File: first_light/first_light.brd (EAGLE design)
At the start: 160 x 100 mm, 56 parts, among them IC1 MC34063AD, J1 DCJ0202, J2 DCJ0202, Q1 ZXMN4A06GTA, U1 STM32F051C6T6, X1 8MHz, Y1 32.768kHz

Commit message: more layout work
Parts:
- moved R7 75.5 mm to (44.6, 72.4), turned to 270 degrees
- moved R11 74.7 mm to (65.0, 69.6)
- moved R12 74.7 mm to (70.5, 69.6)
- moved T2 74.7 mm to (66.5, 72.6)
- moved T3 74.7 mm to (71.9, 72.6)
- moved R10 74.7 mm to (59.6, 69.6)
- moved R13 74.7 mm to (48.9, 69.6)
- moved R8 74.7 mm to (42.5, 72.5)
- moved R9 74.7 mm to (54.2, 69.6)
- moved T1 74.7 mm to (61.1, 72.6)
- moved T4 74.7 mm to (55.7, 72.6)
- moved T5 74.7 mm to (50.3, 72.6)
- moved R2 74.6 mm to (62.8, 89.7)
- moved R3 74.6 mm to (60.2, 89.7)
- moved R4 74.6 mm to (57.7, 89.7)
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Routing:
- net +12V: track 0.00 -> 162.8 mm
- net SSD_B: track 0.00 -> 50.5 mm
- net SSD_G: track 0.00 -> 46.3 mm
- net SSD_A: track 0.00 -> 42.3 mm
- net SSD_C: track 0.00 -> 38.2 mm
- net SSD_L1L2: track 0.00 -> 33.9 mm
- net SSD_F: track 0.00 -> 29.5 mm
- net N$8: track 0.00 -> 24.2 mm
- net N$32: track 0.00 -> 23.7 mm
- net +3V3: track 0.00 -> 17.1 mm
- net N$7: track 0.00 -> 15.9 mm
- net N$28: track 0.00 -> 8.44 mm
- net N$10: track 0.00 -> 7.08 mm
- net N$29: track 0.00 -> 5.98 mm
- net N$13: track 0.00 -> 5.16 mm
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- added copper zone on layer 1, net SWITCH

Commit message: layout work
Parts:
- moved C5 82.0 mm to (122.2, 91.2), turned to 90 degrees
- moved C4 75.4 mm to (117.1, 91.2), turned to 90 degrees
- moved S1 68.3 mm to (117.1, 69.7), turned to 90 degrees
- moved C3 68.2 mm to (112.0, 90.0), turned to 90 degrees
- moved C9 68.1 mm to (114.5, 83.6), turned to 90 degrees
- moved C2 65.8 mm to (114.5, 77.3), turned to 90 degrees
- moved C10 61.3 mm to (109.5, 83.6), turned to 90 degrees
- moved C1 58.8 mm to (109.5, 77.3), turned to 90 degrees
- moved JP1 58.5 mm to (100.6, 95.0), turned to 180 degrees
- moved U1 49.9 mm to (101.8, 81.1), turned to 90 degrees
- moved X1 48.6 mm to (103.1, 67.1), turned to 180 degrees
- moved Y1 39.9 mm to (96.8, 72.2), turned to 90 degrees
- moved R16 35.5 mm to (91.1, 80.2), turned to 180 degrees
- moved R15 32.9 mm to (86.6, 83.6), turned to 180 degrees

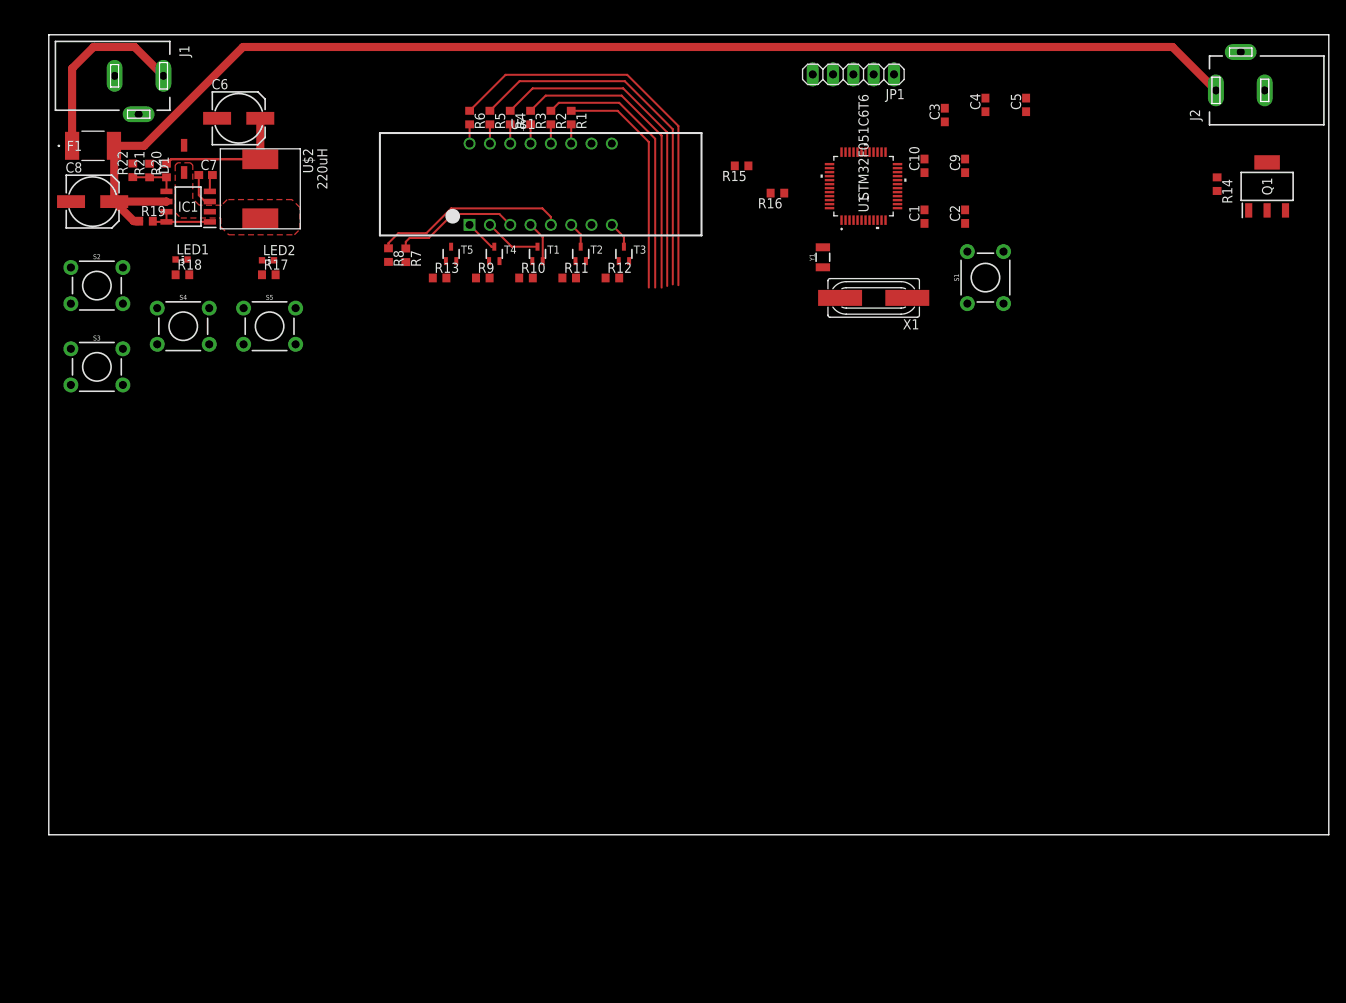
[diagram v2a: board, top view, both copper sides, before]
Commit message: now using esp32 due to no stm available
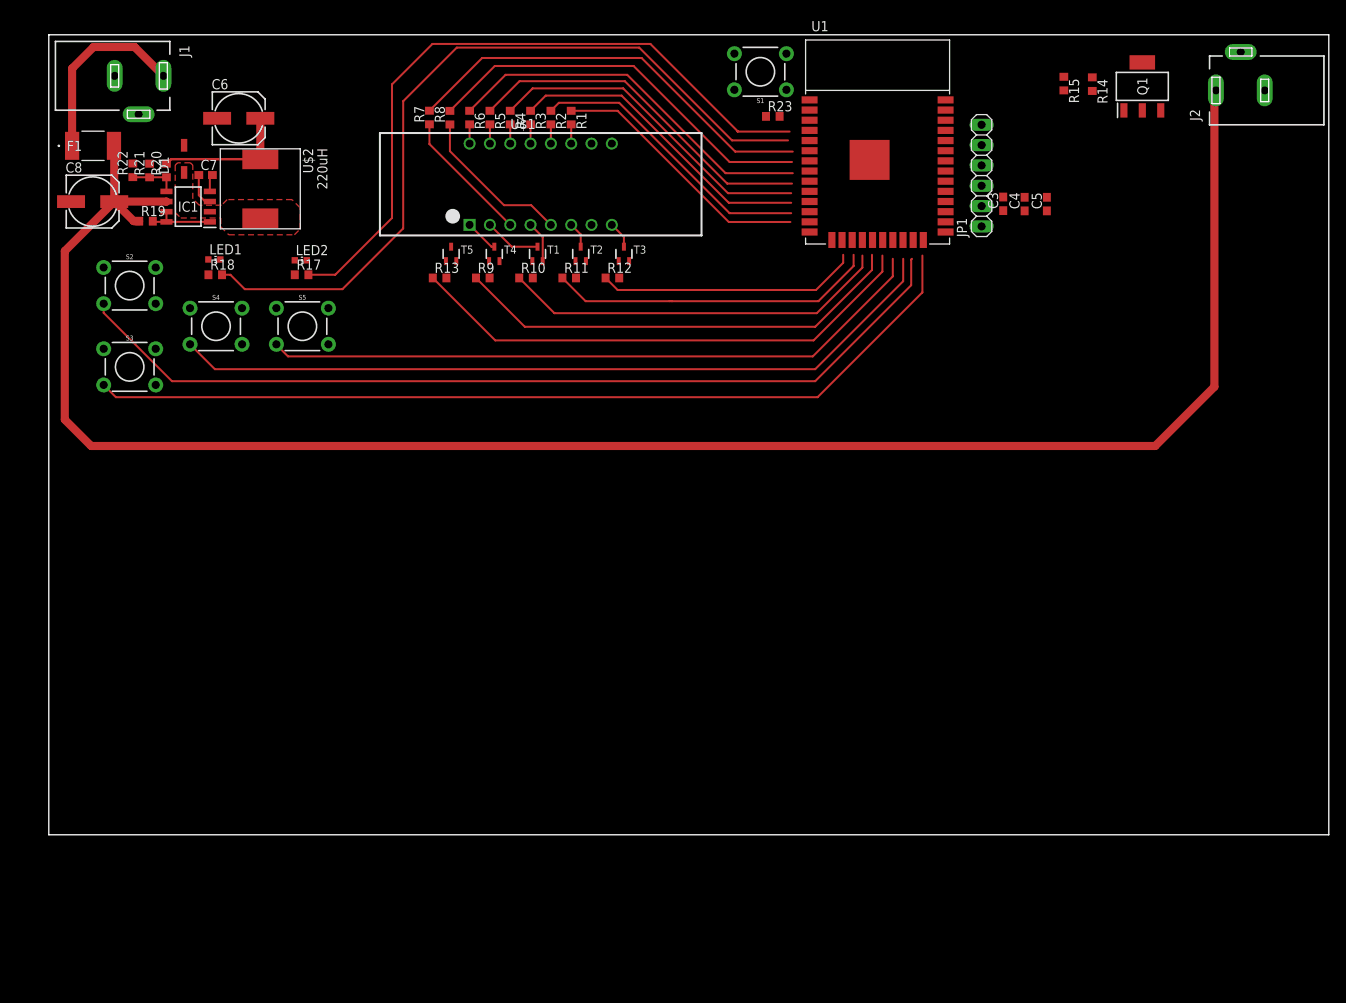
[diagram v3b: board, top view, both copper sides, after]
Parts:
- removed C1, C10, C2, C9: 10pF, rcl:C0603
- removed R16: 10k, rcl:R0603
- removed X1: 8MHz, IQD-Frequency-Products:HC49-4-HSMX
- removed Y1: 32.768kHz, SparkFun-Clocks:CRYSTAL-SMD-3.2X1.5MM
- added R23: 10k, rcl:R0603
- JP1: device pinhead:1X05 -> pinhead:1X06
- U1: value STM32F051C6T6 -> ESP32-WROOM-32D; device STM32F051C6:LQFP48-7X7MM -> ESP32-WROOM-32D:MODULE_ESP32-WROOM-32D
- moved R15 41.6 mm to (126.9, 93.9), turned to 270 degrees
- moved S1 38.1 mm to (89.0, 95.4), turned to 180 degrees
- moved JP1 20.4 mm to (116.6, 82.4), turned to 90 degrees
- moved Q1 20.0 mm to (136.7, 93.5)
- moved R14 20.0 mm to (130.4, 93.8)
- moved R8 18.8 mm to (50.1, 89.6), turned to 90 degrees
- moved R7 17.5 mm to (47.6, 89.7), turned to 90 degrees
- moved C4 13.3 mm to (122.0, 78.8)
- moved C3 13.3 mm to (119.3, 78.9)
- moved C5 12.7 mm to (124.8, 78.8)
- moved U1 5.79 mm to (103.6, 86.6), turned to 0 degrees
- moved LED1 4.10 mm to (20.7, 71.9)
- moved LED2 4.10 mm to (31.5, 71.8)
- moved R17 4.10 mm to (31.6, 70.0)
- moved R18 4.10 mm to (20.8, 70.0)
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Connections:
- removed net N$14: C1.1, U1.6, X1.1
- removed net N$20: C2.1, U1.5, X1.2
- removed net N$25: R16.1, U1.44
- removed net N$30: C9.1, U1.4, Y1.P$1
- removed net N$31: C10.1, U1.3, Y1.P$2
- removed net SWCLK: JP1.3, U1.37
- removed net SWDIO: JP1.2, U1.34
- removed net VBAT: U1.1
- new net IO0: JP1.4
- new net RXD0: JP1.5, U1.34
- new net TXD0: JP1.6, U1.35
- net !RST: now also R23.1, U1.3; no longer U1.7
- net +3V3: now also JP1.2, R23.2, U1.2; no longer JP1.4, U1.24, U1.48, U1.9
- net BTN_DN: now also U1.24; no longer U1.12
- net BTN_L: now also U1.22; no longer U1.11
- net BTN_R: now also U1.21; no longer U1.10
- net BTN_UP: now also U1.23; no longer U1.13
- net GND: now also JP1.3, U1.1, U1.15, U1.38, U1.39; no longer C1.2, C10.2, C2.2, C9.2, JP1.5, R16.2, U1.23, U1.47, U1.8
- net LED_ALM: now also U1.5; no longer U1.15
- net LED_SET: now also U1.4; no longer U1.14
- net SSD_A: now also U1.10; no longer U1.42
- net SSD_B: now also U1.8; no longer U1.40
- net SSD_BLANK: now also U1.20
- net SSD_C: now also U1.11; no longer U1.43
- net SSD_D1: now also U1.19
- net SSD_D2: now also U1.18
- net SSD_D3: now also U1.17
- net SSD_D4: now also U1.16
- net SSD_F: now also U1.13; no longer U1.46
- net SSD_G: now also U1.9; no longer U1.41
- net SSD_L1L2: now also U1.12; no longer U1.45
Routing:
- net BTN_UP: track 0.00 -> 113.9 mm
- net BTN_DN: track 0.00 -> 113.0 mm
- net LED_ALM: track 0.00 -> 98.1 mm
- net BTN_L: track 0.00 -> 97.8 mm
- net LED_SET: track 0.00 -> 86.5 mm
- net BTN_R: track 0.00 -> 84.1 mm
- net +12V: track 162.8 -> 232.7 mm
- net SSD_BLANK: track 0.00 -> 65.0 mm
- net SSD_D1: track 0.00 -> 56.9 mm
- net SSD_D: track 0.00 -> 53.0 mm
- net SSD_E: track 0.00 -> 50.1 mm
- net SSD_D2: track 0.00 -> 48.6 mm
- net SSD_D3: track 0.00 -> 40.8 mm
- net SSD_D4: track 0.00 -> 32.7 mm
- net N$8: track 24.2 -> 19.8 mm
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
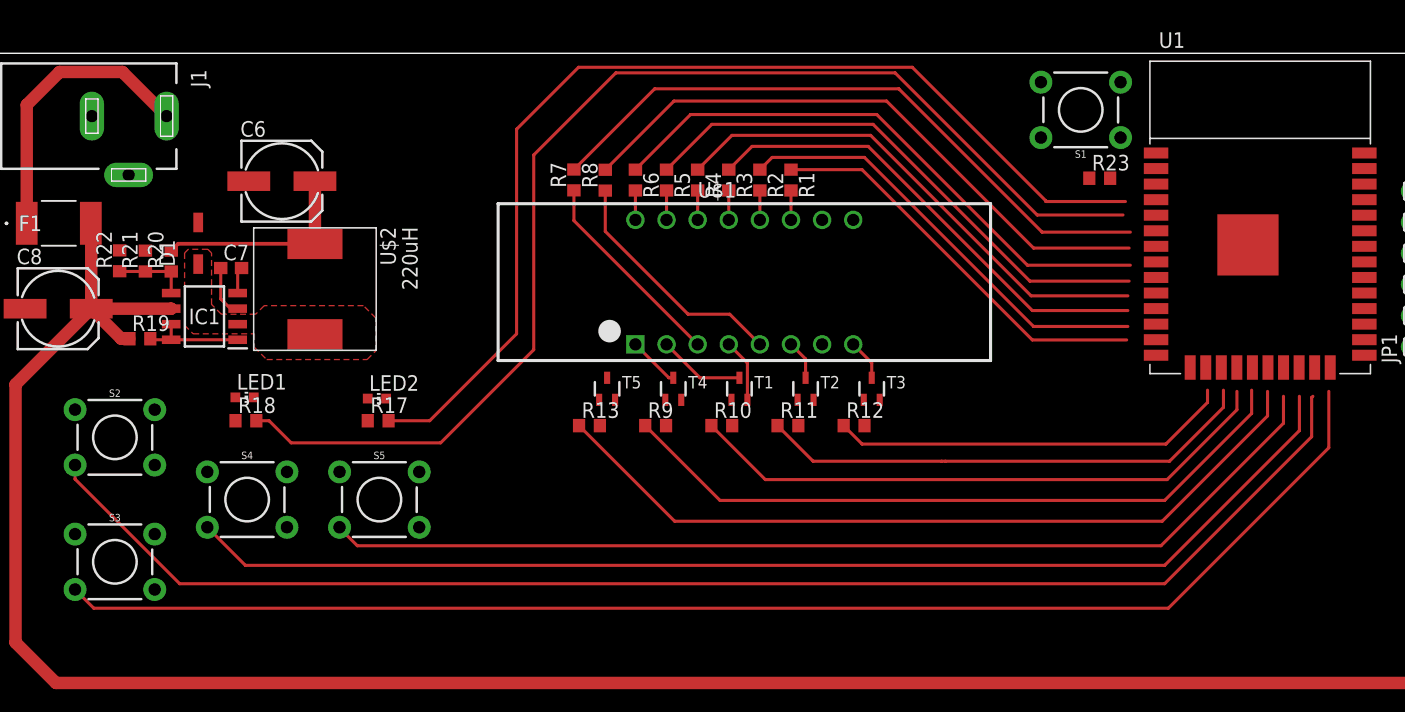
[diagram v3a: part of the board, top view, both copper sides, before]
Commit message: wired up ssd to esp
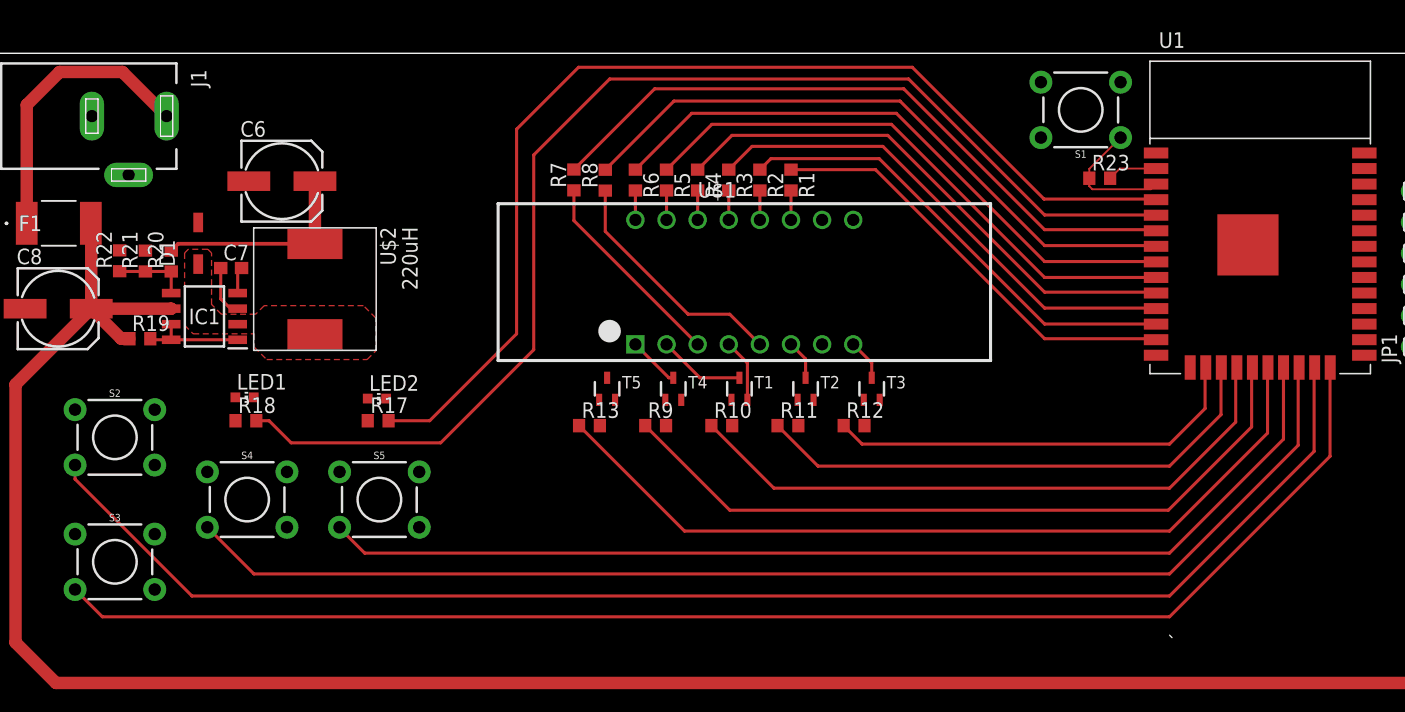
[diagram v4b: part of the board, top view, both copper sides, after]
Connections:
- net SSD_D: now also U1.6
- net SSD_E: now also U1.7
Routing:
- net !RST: track 0.00 -> 10.8 mm
- net +3V3: track 17.1 -> 21.1 mm
- net BTN_UP: track 113.9 -> 118.0 mm
- net BTN_R: track 84.1 -> 87.7 mm
- net BTN_L: track 97.8 -> 101.4 mm
- net SSD_BLANK: track 65.0 -> 68.4 mm
- net SSD_D1: track 56.9 -> 60.1 mm
- net SSD_D2: track 48.6 -> 51.6 mm
- net BTN_DN: track 113.0 -> 116.0 mm
- net LED_SET: track 86.5 -> 88.9 mm
- net SSD_F: track 33.2 -> 35.5 mm
- net SSD_D3: track 40.8 -> 43.2 mm
- net LED_ALM: track 98.1 -> 100.4 mm
- net SSD_C: track 38.9 -> 41.2 mm
- net SSD_A: track 41.7 -> 43.9 mm
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
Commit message: last adjustments before new layout
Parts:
- moved J2 105.8 mm to (87.7, 6.85)
- moved R14 88.8 mm to (88.5, 15.5)
- moved Q1 86.6 mm to (95.0, 17.6)
- moved R15 80.8 mm to (100.4, 17.6)
- moved C4 56.5 mm to (101.3, 26.2)
- moved C3 49.2 mm to (100.0, 33.6)
- moved JP1 49.2 mm to (97.3, 37.1)
- moved U1 49.2 mm to (84.3, 41.3)
- moved LED1 48.2 mm to (18.4, 23.8)
- moved S2 48.2 mm to (7.81, 20.6)
- moved S3 48.2 mm to (7.81, 10.4)
- moved S4 48.2 mm to (18.6, 15.5)
- moved S5 48.2 mm to (29.4, 15.5)
- moved LED2 48.2 mm to (29.2, 23.7)
- moved R17 48.2 mm to (29.3, 21.9)
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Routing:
- net +12V: track 232.7 -> 132.1 mm
- net BTN_UP: track 118.0 -> 100.9 mm
- net BTN_R: track 87.7 -> 70.6 mm
- net BTN_L: track 101.4 -> 84.3 mm
- net BTN_DN: track 116.0 -> 99.0 mm
- net LED_SET: track 88.9 -> 76.2 mm
- net LED_ALM: track 100.4 -> 87.7 mm
- net SSD_D2: track 51.6 -> 40.1 mm
- net SSD_D4: track 34.7 -> 23.1 mm
- net SSD_BLANK: track 68.4 -> 56.9 mm
- net SSD_D3: track 43.2 -> 31.6 mm
- net SSD_D1: track 60.1 -> 48.5 mm
- net SSD_F: track 35.5 -> 24.9 mm
- net SSD_D: track 55.1 -> 44.5 mm
- net SSD_E: track 52.2 -> 41.8 mm
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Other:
- board size 160 x 100 mm -> 100 x 55 mm

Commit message: working on new layout
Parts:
- moved R15 92.9 mm to (13.5, -15.2)
- moved J2 85.2 mm to (3.85, -8.49), turned to 0 degrees
- moved Q1 79.7 mm to (20.2, -9.85)
- moved R14 77.2 mm to (14.0, -4.77)
- moved JP1 56.8 mm to (47.7, 9.40), turned to 270 degrees
- moved U1 46.6 mm to (52.5, 7.20), turned to 180 degrees
- moved R7 20.1 mm to (53.3, 30.0), turned to 270 degrees
- moved R6 18.3 mm to (55.7, 30.1), turned to 90 degrees
- moved R5 18.2 mm to (58.2, 30.1), turned to 90 degrees
- moved R4 18.2 mm to (60.7, 30.1), turned to 90 degrees
- moved R3 18.2 mm to (63.2, 30.1), turned to 90 degrees
- moved R2 18.2 mm to (65.7, 30.1), turned to 90 degrees
- moved R1 18.1 mm to (68.2, 30.1), turned to 90 degrees
- moved R8 16.9 mm to (51.1, 30.1), turned to 270 degrees
- moved T3 15.8 mm to (48.4, 32.7)
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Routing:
- net +12V: track 132.1 -> 26.4 mm
- net BTN_DN: track 99.0 -> 0.00 mm
- net BTN_UP: track 100.9 -> 12.5 mm
- net BTN_L: track 84.3 -> 0.00 mm
- net LED_SET: track 76.2 -> 3.19 mm
- net LED_ALM: track 87.7 -> 16.4 mm
- net BTN_R: track 70.6 -> 0.00 mm
- net SSD_BLANK: track 56.9 -> 0.00 mm
- net SSD_D1: track 48.5 -> 0.00 mm
- net SSD_D: track 44.5 -> 0.00 mm
- net SSD_E: track 41.8 -> 0.00 mm
- net SSD_D2: track 40.1 -> 0.00 mm
- net SSD_B: track 39.1 -> 0.00 mm
- net SSD_G: track 36.3 -> 0.00 mm
- net SSD_A: track 33.6 -> 0.00 mm
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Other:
- board size 100 x 55 mm -> 100 x 50 mm

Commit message: layout and routing
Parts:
- moved R15 80.7 mm to (91.7, 4.70), turned to 90 degrees
- moved J2 80.0 mm to (81.5, 11.0)
- moved R14 75.8 mm to (89.3, 4.77), turned to 90 degrees
- moved Q1 74.3 mm to (91.5, 10.9)
- moved C5 50.5 mm to (68.4, 2.67)
- moved C3 47.7 mm to (63.7, 2.67)
- moved S1 43.8 mm to (81.8, 21.4), turned to 0 degrees
- moved C4 42.4 mm to (66.0, 2.66), turned to 270 degrees
- moved R23 35.2 mm to (75.3, 23.1), turned to 270 degrees
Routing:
- net N$13: track 0.00 -> 32.1 mm
- net N$1: track 0.00 -> 26.9 mm
- net N$2: track 0.00 -> 26.9 mm
- net N$3: track 0.00 -> 26.6 mm
- net N$4: track 0.00 -> 25.9 mm
- net N$5: track 0.00 -> 25.4 mm
- net N$6: track 0.00 -> 25.1 mm
- net SSD_D1: track 0.00 -> 24.2 mm
- net SSD_D2: track 0.00 -> 21.6 mm
- net SSD_D3: track 0.00 -> 18.9 mm
- net SSD_D4: track 0.00 -> 16.3 mm
- net N$12: track 0.00 -> 15.1 mm, vias 0 -> 1
- net N$11: track 0.00 -> 13.7 mm
- net N$7: track 0.00 -> 11.7 mm, vias 0 -> 1
- net !RST: track 11.5 -> 0.00 mm
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- added copper zone on layer 1, net GND
- added copper zone on layer 16, net GND

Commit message: finished layout and routing
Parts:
- moved C5 0.24 mm to (68.3, 2.43), turned to 270 degrees
- moved C3 0.24 mm to (63.7, 2.43), turned to 270 degrees
- moved C4 0.20 mm to (66.0, 2.46)
- moved R15 0.10 mm to (91.7, 4.80)
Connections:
- net BTN_DN: now also U1.22; no longer U1.24
- net BTN_L: now also U1.23; no longer U1.22
- net BTN_R: now also U1.24; no longer U1.21
- net BTN_UP: now also U1.21; no longer U1.23
- net IO0: now also U1.25
- net LED_PWM: now also U1.14
- net SSD_A: now also U1.9; no longer U1.10
- net SSD_B: now also U1.11; no longer U1.8
- net SSD_C: now also U1.8; no longer U1.11
- net SSD_D: now also U1.12; no longer U1.6
- net SSD_E: now also U1.13; no longer U1.7
- net SSD_F: now also U1.6; no longer U1.13
- net SSD_G: now also U1.10; no longer U1.9
- net SSD_L1L2: now also U1.7; no longer U1.12
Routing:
- net +12V: track 26.4 -> 117.4 mm, vias 0 -> 1
- net +3V3: track 17.1 -> 105.4 mm, vias 0 -> 2
- net BTN_DN: track 0.00 -> 58.2 mm
- net !RST: track 0.00 -> 55.0 mm, vias 0 -> 1
- net BTN_L: track 0.00 -> 45.7 mm
- net BTN_UP: track 12.5 -> 56.9 mm
- net LED_PWM: track 0.00 -> 40.8 mm, vias 0 -> 2
- net LED_SET: track 3.19 -> 37.1 mm, vias 0 -> 2
- net BTN_R: track 0.00 -> 33.3 mm
- net LED_ALM: track 16.4 -> 48.4 mm, vias 0 -> 2
- net SSD_BLANK: track 0.00 -> 25.6 mm
- net SSD_F: track 0.00 -> 24.7 mm
- net SSD_L1L2: track 0.00 -> 22.8 mm
- net SSD_G: track 0.00 -> 22.7 mm
- net SSD_C: track 0.00 -> 22.0 mm
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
